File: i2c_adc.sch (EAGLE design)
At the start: 15 parts, among them IC1 ESP-12E/F, U8 NCP1117LPST50T3G

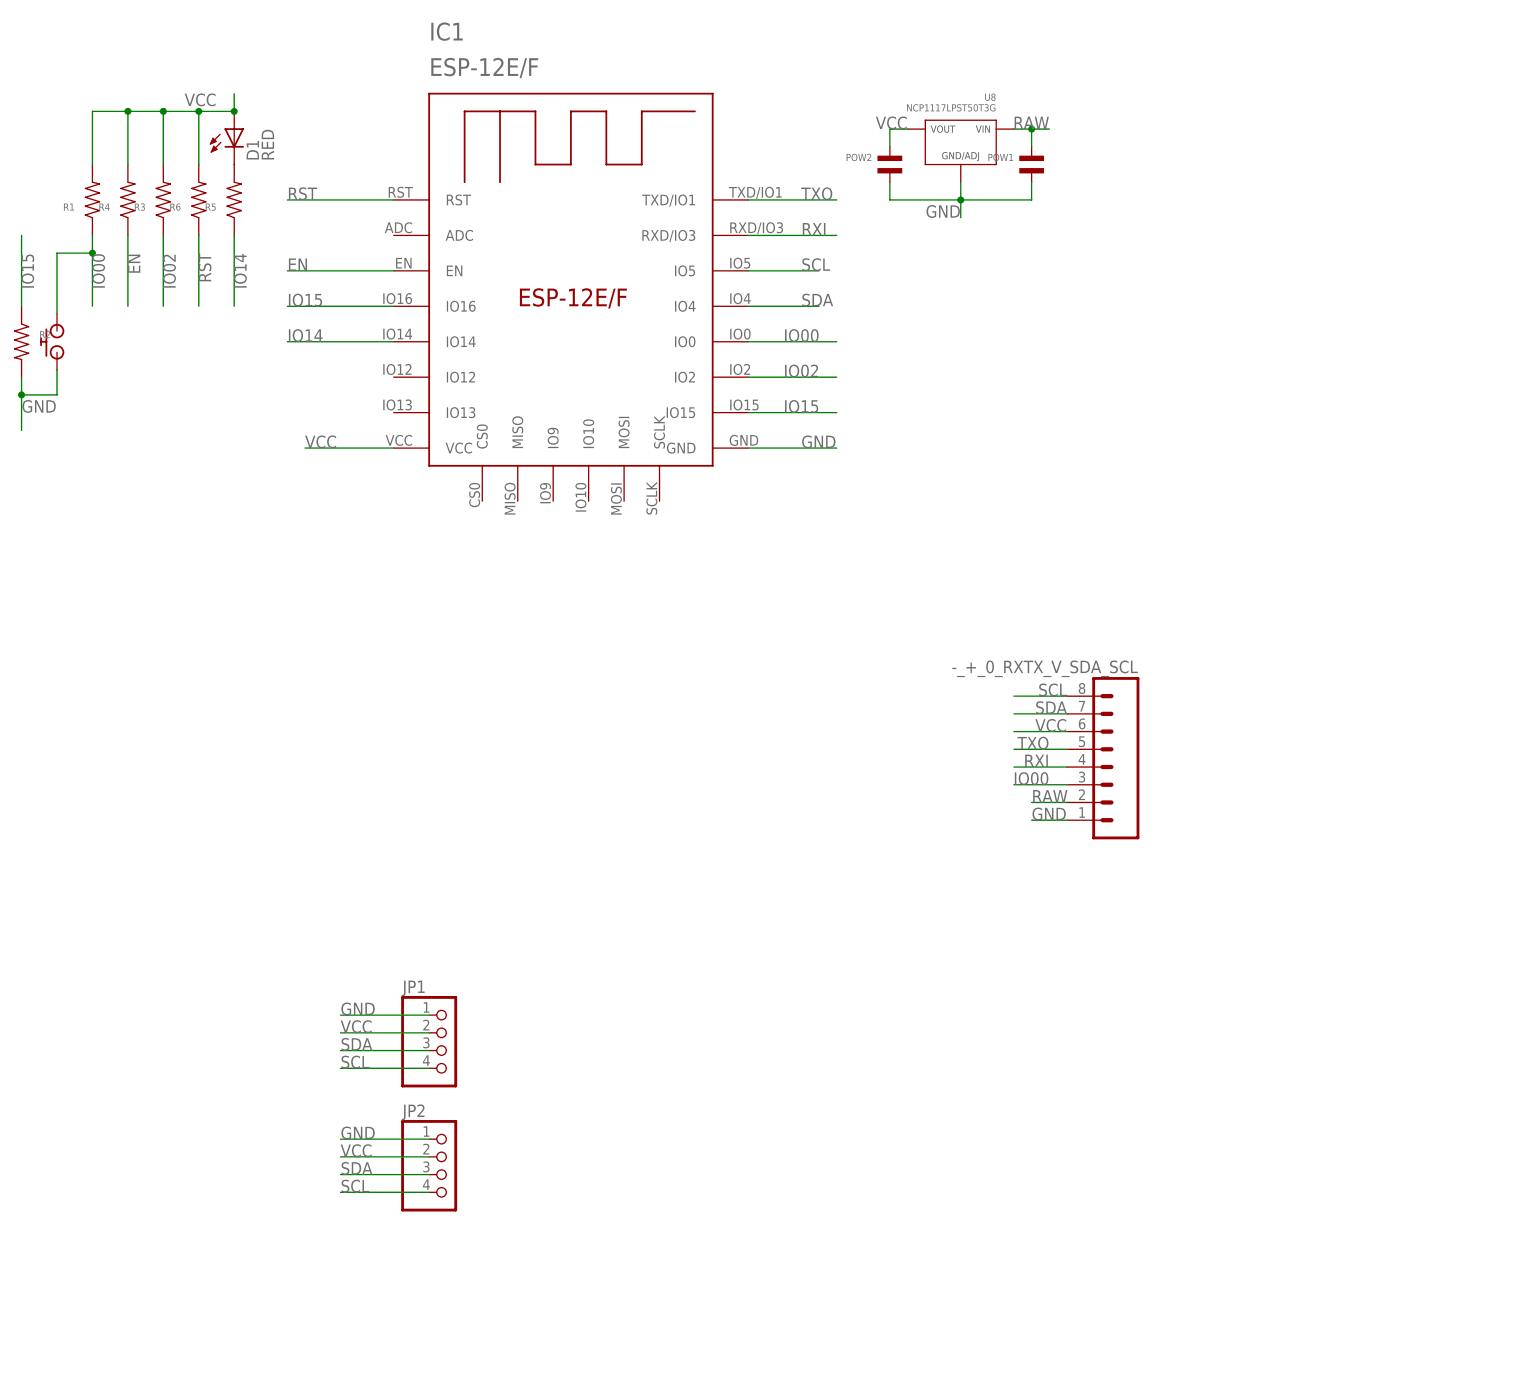
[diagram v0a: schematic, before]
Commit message: Spin i2c_adc board, add jst connectors, 6 voltage divider channels
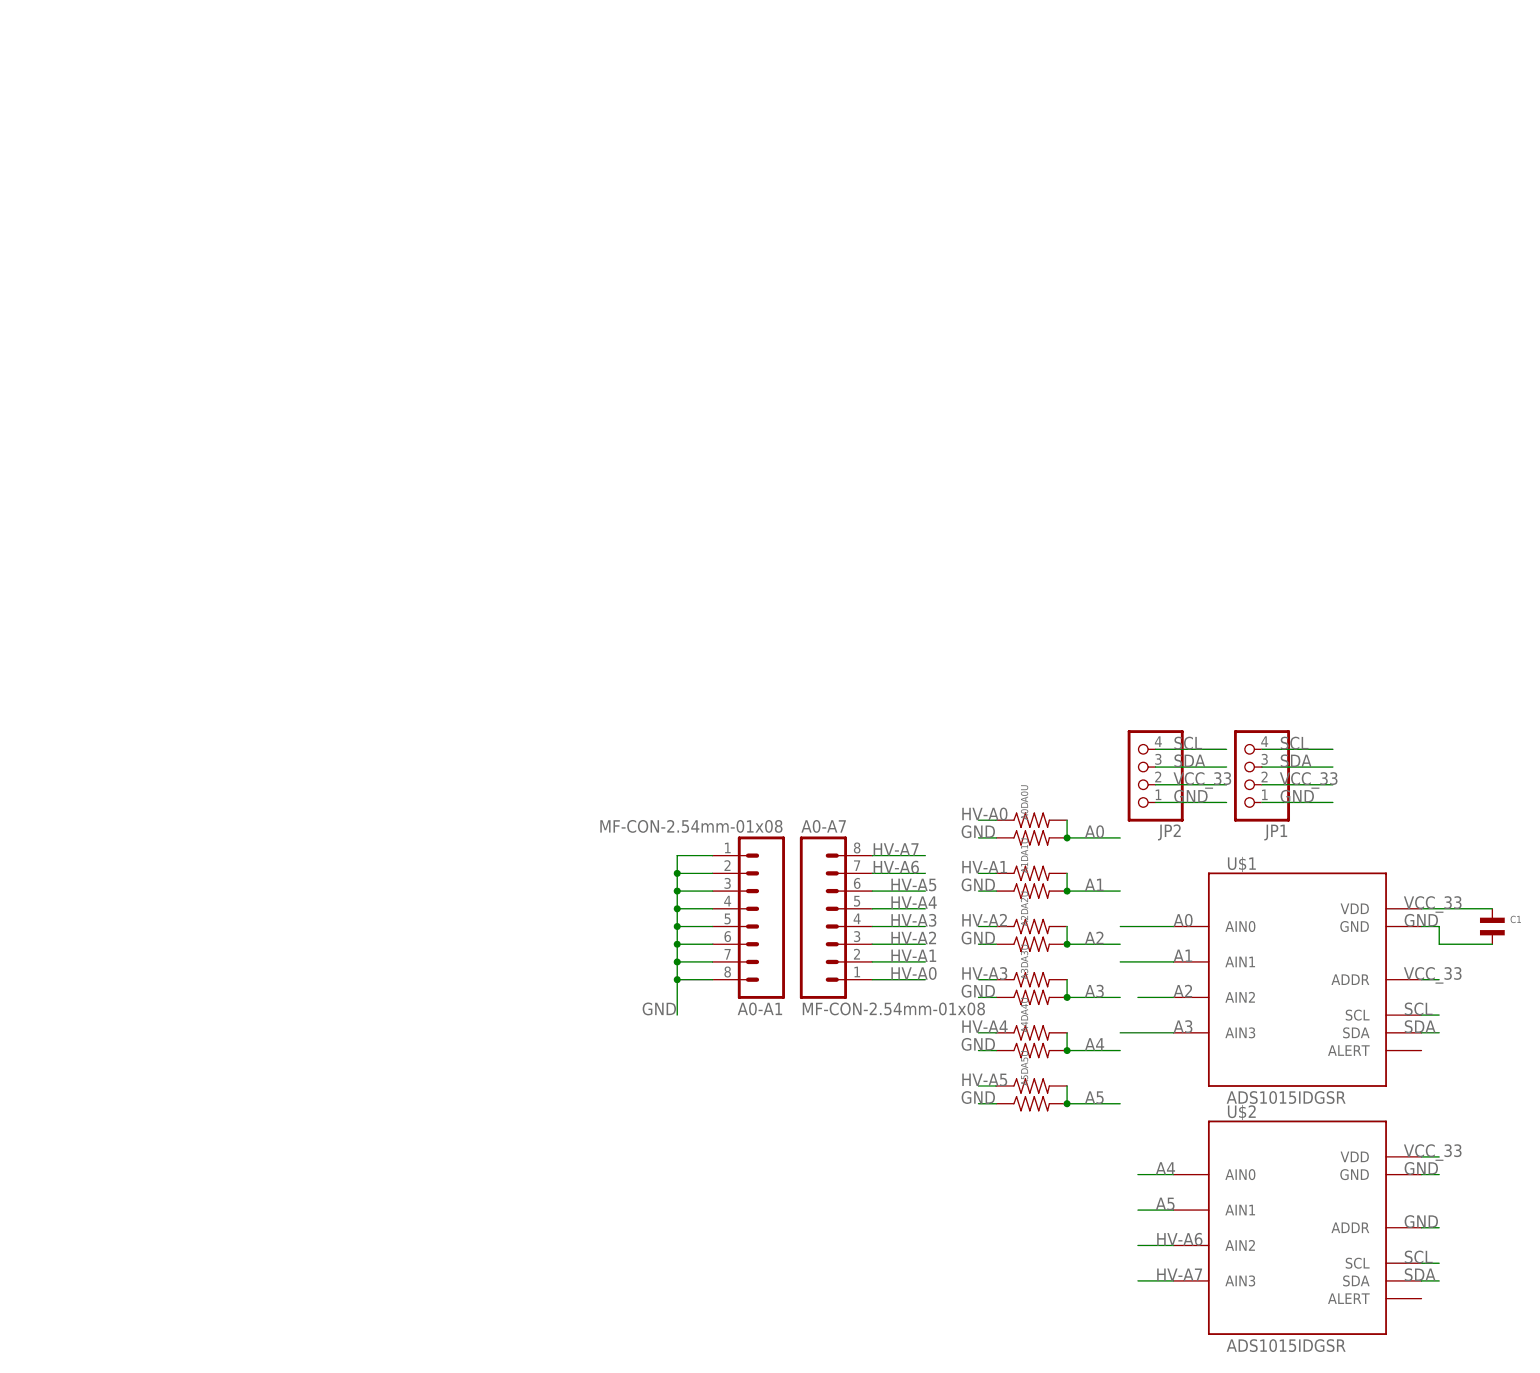
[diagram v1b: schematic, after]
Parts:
- removed -_+_0_RXTX_V_SDA_SCL: MF-CON-2.54mm-01x08, SparkFun-Connectors:M081X08
- removed D1: RED, 00jim:LED-RED0603
- removed IC1: ESP-12E/F, esp-12e-f:ESP-12E/F
- removed POW1, POW2: (no value), MF_Passives:CAPACITOR_NP_1210
- removed R1, R2, R3, R4, R5, R6: (no value), 00jim:RESISTOR_0603
- removed U8: NCP1117LPST50T3G, MF_IC_Power:NCP1117LPST50T3G
- added A0-A1, A0-A7: MF-CON-2.54mm-01x08, SparkFun-Connectors:M081X08
- added A0D, A0U, A1D, A1U, A2D, A2U, A3D, A3U, A4D, A4U, A5D, A5U: (no value), MF_Passives:RESISTOR_0603
- added C1: (no value), 00jim:CAPACITOR_NP_1206
- added U$2: ADS1015IDGSR, bt_adc:ADS1015IDGT
- JP1, JP2: device microbuilder:HEADER-1X41MMPADS -> 00jim:HEADER-1X41MMPADS
- U$1: value AMAZON_BUTTON -> ADS1015IDGSR; device 00jim:AMAZON_BUTTON -> bt_adc:ADS1015IDGT
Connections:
- removed net EN: IC1.EN, R4.P$1
- removed net IO00: -_+_0_RXTX_V_SDA_SCL.3, IC1.IO0, R1.P$1, U$1.P$1
- removed net IO02: IC1.IO2, R3.P$1
- removed net IO14: IC1.IO14, R5.P$1
- removed net IO15: IC1.IO15, IC1.IO16, R2.P$1
- removed net N$2: D1.C, R5.P$2
- removed net RAW: -_+_0_RXTX_V_SDA_SCL.2, POW1.P$1, U8.VIN
- removed net RST: IC1.RST, R6.P$1
- removed net RXI: -_+_0_RXTX_V_SDA_SCL.4, IC1.RXD/IO3
- removed net TXO: -_+_0_RXTX_V_SDA_SCL.5, IC1.TXD/IO1
- removed net VCC: -_+_0_RXTX_V_SDA_SCL.6, D1.A, IC1.VCC, JP1.2, JP2.2, POW2.P$1, R1.P$2, R3.P$2, R4.P$2, R6.P$2, U8.VOUT
- new net A0: A0D.P$2, A0U.P$2, U$1.AIN0
- new net A1: A1D.P$2, A1U.P$2, U$1.AIN1
- new net A2: A2D.P$2, A2U.P$2, U$1.AIN2
- new net A3: A3D.P$2, A3U.P$2, U$1.AIN3
- new net A4: A4D.P$2, A4U.P$2, U$2.AIN0
- new net A5: A5D.P$2, A5U.P$2, U$2.AIN1
- new net HV-A0: A0-A7.1, A0U.P$1
- new net HV-A1: A0-A7.2, A1U.P$1
- new net HV-A2: A0-A7.3, A2U.P$1
- new net HV-A3: A0-A7.4, A3U.P$1
- new net HV-A4: A0-A7.5, A4U.P$1
- new net HV-A5: A0-A7.6, A5U.P$1
- new net HV-A6: A0-A7.7, U$2.AIN2
- new net HV-A7: A0-A7.8, U$2.AIN3
- new net VCC_33: C1.P$1, JP1.2, JP2.2, U$1.ADDR, U$1.VDD, U$2.VDD
- net GND: now also A0-A1.1, A0-A1.2, A0-A1.3, A0-A1.4, A0-A1.5, A0-A1.6, A0-A1.7, A0-A1.8, A0D.P$1, A1D.P$1, A2D.P$1, A3D.P$1, A4D.P$1, A5D.P$1, C1.P$2, U$1.GND, U$2.ADDR, U$2.GND; no longer -_+_0_RXTX_V_SDA_SCL.1, IC1.GND, POW1.P$2, POW2.P$2, R2.P$2, U$1.P$2, U8.GND/ADJ
- net SCL: now also U$1.SCL, U$2.SCL; no longer -_+_0_RXTX_V_SDA_SCL.8, IC1.IO5
- net SDA: now also U$1.SDA, U$2.SDA; no longer -_+_0_RXTX_V_SDA_SCL.7, IC1.IO4
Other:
- moved on the sheet: JP1, JP2
